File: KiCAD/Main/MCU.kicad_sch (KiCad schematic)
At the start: 26 parts, among them Q4 2N7002, SW1 RESET, SW2 USER, U4 STM32H750VBTx, Y2 SiT8008xx-2x-xxE (25MHz)

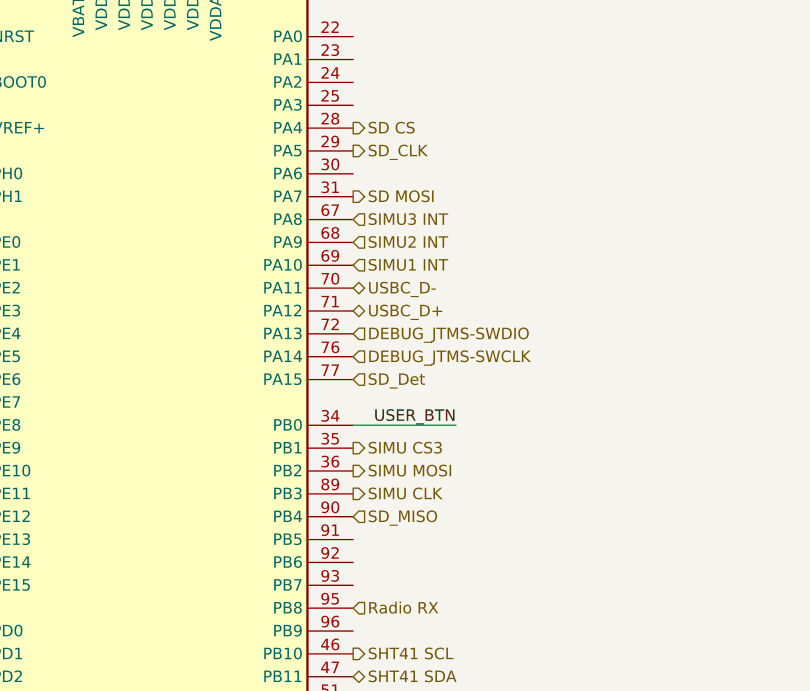
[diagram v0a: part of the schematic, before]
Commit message: Moved MISO1 to better position
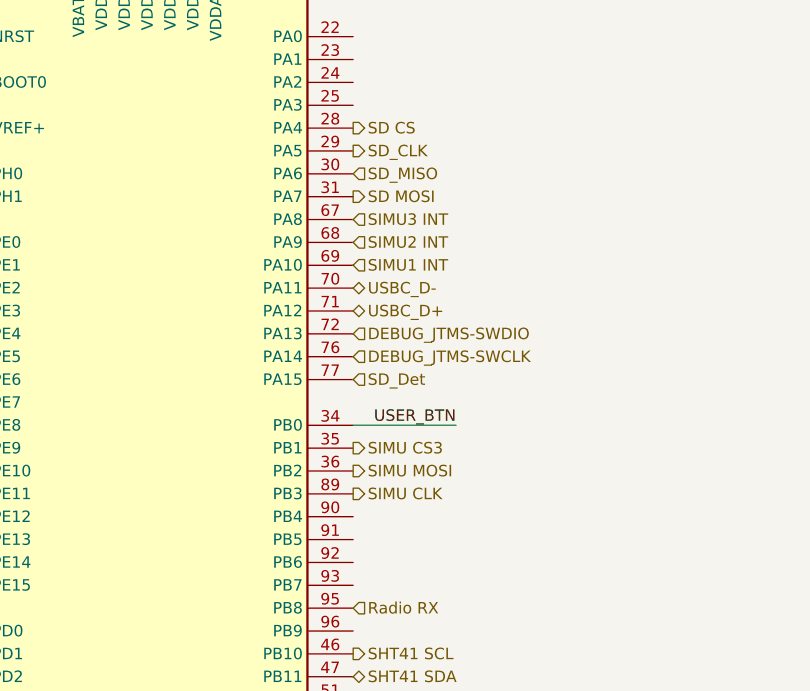
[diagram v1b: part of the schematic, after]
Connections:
- net SD_MISO: now also U4.30 (PA6); no longer U4.90 (PB4)
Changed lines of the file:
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@@
+		)
+	)
+	(hierarchical_label "SD_MISO"
+		(shape input)
+		(at 124.46 57.15 0)
+		(effects
+			(font
+				(size 1.27 1.27)
+			)
+			(justify left)
 		)
 	)
@@
 		(effects
 			(font
-				(size 1.27 1.27)
-			)
-			(justify left)
-		)
-	)
-	(hierarchical_label "SD_MISO"
-		(shape input)
-		(at 124.46 95.25 0)
-		(effects
-			(font

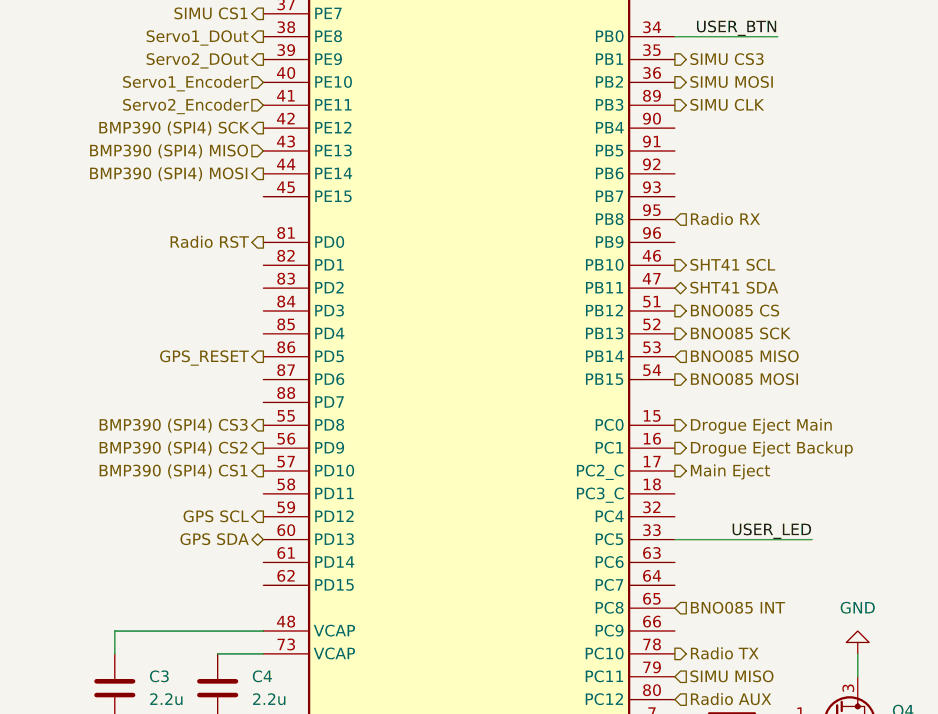
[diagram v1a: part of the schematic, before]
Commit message: Moved GPS I2C to more optimal location
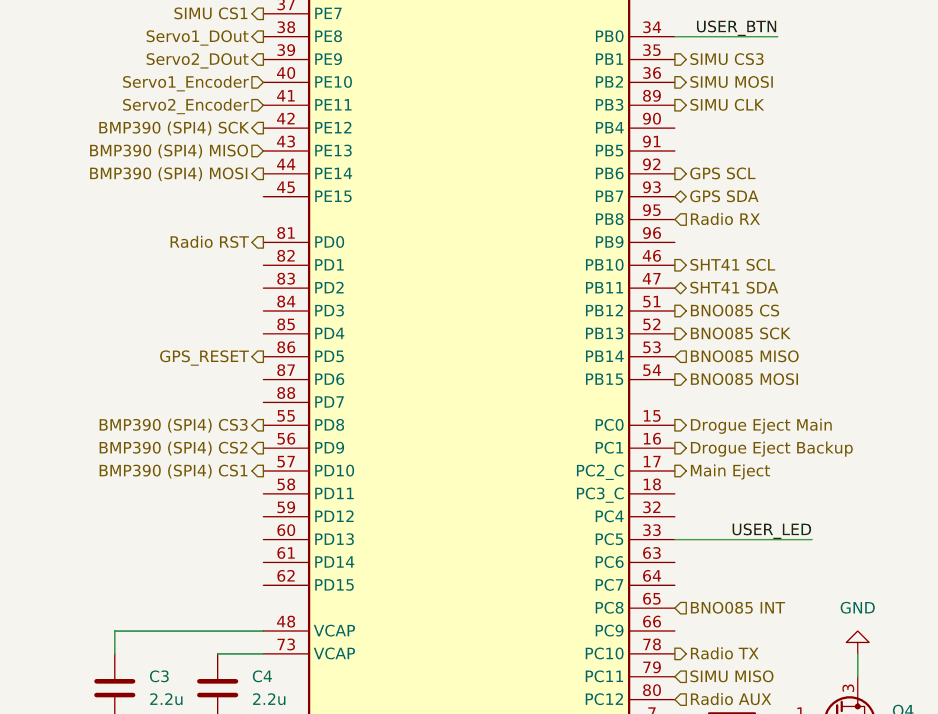
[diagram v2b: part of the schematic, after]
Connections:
- net GPS SCL: now also U4.92 (PB6); no longer U4.59 (PD12)
- net GPS SDA: now also U4.93 (PB7); no longer U4.60 (PD13)
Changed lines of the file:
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@@
-		)
-	)
-	(hierarchical_label "GPS SDA"
-		(shape bidirectional)
-		(at 78.74 140.97 180)
-		(effects
-			(font
-				(size 1.27 1.27)
-			)
-			(justify right)
 		)
 	)
@@
 		)
 	)
+	(hierarchical_label "GPS SCL"
+		(shape output)
+		(at 124.46 100.33 0)
+		(effects
+			(font
+				(size 1.27 1.27)
+			)
+			(justify left)
+		)
+	)
 	(hierarchical_label "BMP390 (SPI4) CS2"
 		(shape output)
@@
 		)
 	)
-	(hierarchical_label "GPS SCL"
-		(shape output)
-		(at 78.74 138.43 180)
-		(effects
-			(font
-				(size 1.27 1.27)
-			)
-			(justify right)
-		)
-	)
 	(hierarchical_label "SD_Det"
 		(shape input)
@@
 		)
 	)
+	(hierarchical_label "GPS SDA"
+		(shape bidirectional)
+		(at 124.46 102.87 0)
+		(effects
+			(font
+				(size 1.27 1.27)
+			)
+			(justify left)
+		)
+	)

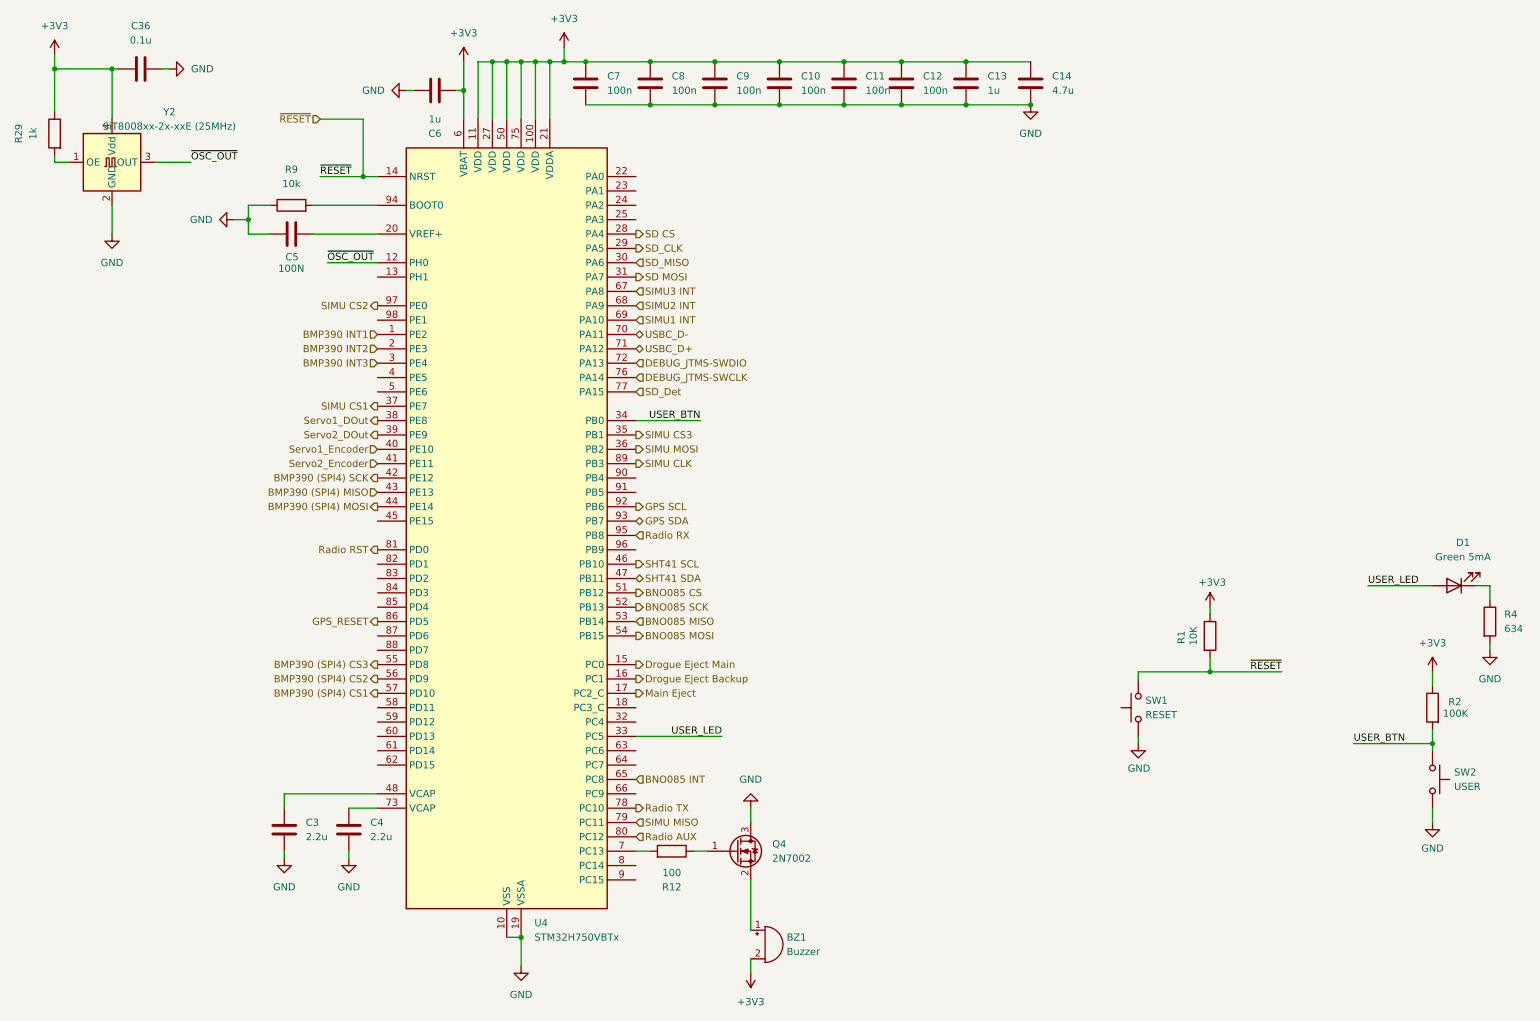
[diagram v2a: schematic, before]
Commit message: Moved around some more pins for easier routing
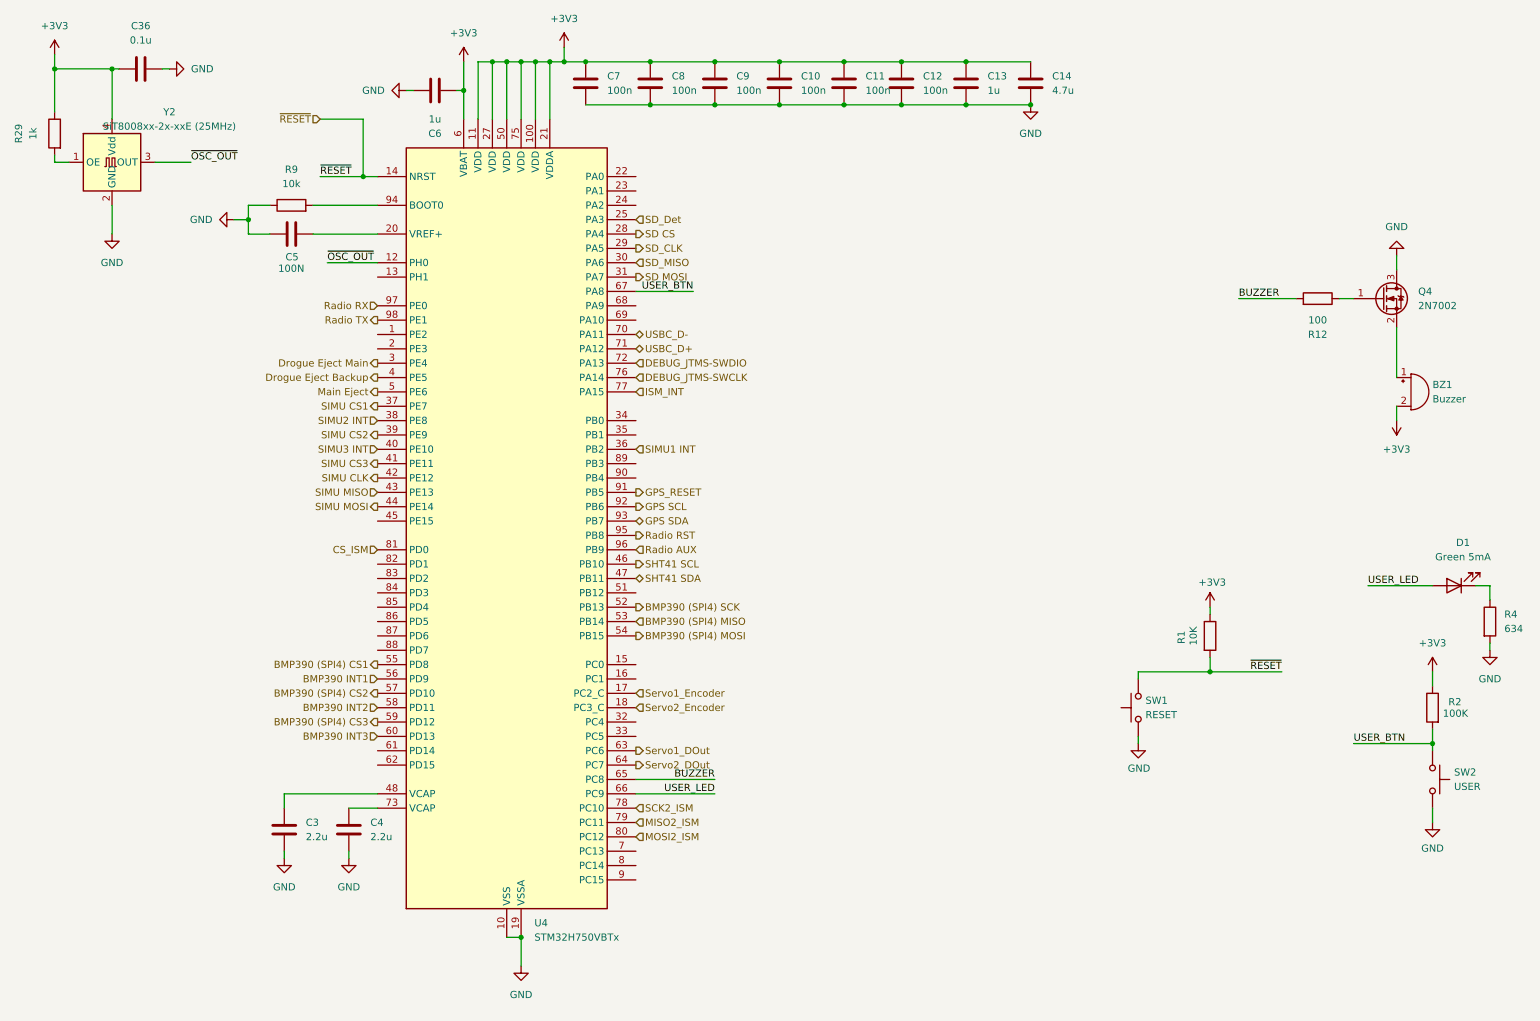
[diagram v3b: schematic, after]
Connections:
- net BNO085 MISO is gone; now on net BMP390 (SPI4) MISO: U4.53 (PB14)
- net BNO085 MOSI is gone; now on net BMP390 (SPI4) MOSI: U4.54 (PB15)
- net BNO085 SCK is gone; now on net BMP390 (SPI4) SCK: U4.52 (PB13)
- net BMP390 (SPI4) CS1: now also U4.55 (PD8); no longer U4.57 (PD10)
- net BMP390 (SPI4) CS2: now also U4.57 (PD10); no longer U4.56 (PD9)
- net BMP390 (SPI4) CS3: now also U4.59 (PD12); no longer U4.55 (PD8)
- net BMP390 (SPI4) MISO: no longer U4.43 (PE13)
- net BMP390 (SPI4) MOSI: no longer U4.44 (PE14)
- net BMP390 (SPI4) SCK: no longer U4.42 (PE12)
- net BMP390 INT1: now also U4.56 (PD9); no longer U4.1 (PE2)
- net BMP390 INT2: now also U4.58 (PD11); no longer U4.2 (PE3)
- net BMP390 INT3: now also U4.60 (PD13); no longer U4.3 (PE4)
- net Drogue Eject Backup: now also U4.4 (PE5); no longer U4.16 (PC1)
- net Drogue Eject Main: now also U4.3 (PE4); no longer U4.15 (PC0)
- net GPS_RESET: now also U4.91 (PB5); no longer U4.86 (PD5)
- net Main Eject: now also U4.5 (PE6); no longer U4.17 (PC2_C)
- net Radio AUX: now also U4.96 (PB9); no longer U4.80 (PC12)
- net Radio RST: now also U4.95 (PB8); no longer U4.81 (PD0)
- net Radio RX: now also U4.97 (PE0); no longer U4.95 (PB8)
- net Radio TX: now also U4.98 (PE1); no longer U4.78 (PC10)
- net SD_Det: now also U4.25 (PA3); no longer U4.77 (PA15)
- net SIMU CLK: now also U4.42 (PE12); no longer U4.89 (PB3)
- net SIMU CS2: now also U4.39 (PE9); no longer U4.97 (PE0)
- net SIMU CS3: now also U4.41 (PE11); no longer U4.35 (PB1)
- net SIMU MISO: now also U4.43 (PE13); no longer U4.79 (PC11)
- net SIMU MOSI: now also U4.44 (PE14); no longer U4.36 (PB2)
- net SIMU1 INT: now also U4.36 (PB2); no longer U4.69 (PA10)
- net SIMU2 INT: now also U4.38 (PE8); no longer U4.68 (PA9)
- net SIMU3 INT: now also U4.40 (PE10); no longer U4.67 (PA8)
- net Servo1_DOut: now also U4.63 (PC6); no longer U4.38 (PE8)
- net Servo1_Encoder: now also U4.17 (PC2_C); no longer U4.40 (PE10)
- net Servo2_DOut: now also U4.64 (PC7); no longer U4.39 (PE9)
- net Servo2_Encoder: now also U4.18 (PC3_C); no longer U4.41 (PE11)
- net USER_BTN: now also U4.67 (PA8); no longer U4.34 (PB0)
- net USER_LED: now also U4.66 (PC9); no longer U4.33 (PC5)
- net at U4.7 (PC13): no longer R12.2
- net BNO085 CS: no longer names the net of U4.51 (PB12)
- net BNO085 INT renamed BUZZER
- net BUZZER: now also R12.2
- new net CS_ISM: U4.81 (PD0)
- new net ISM_INT: U4.77 (PA15)
- new net MISO2_ISM: U4.79 (PC11)
- new net MOSI2_ISM: U4.80 (PC12)
- new net SCK2_ISM: U4.78 (PC10)
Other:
- moved on the sheet: BZ1, Q4, R12

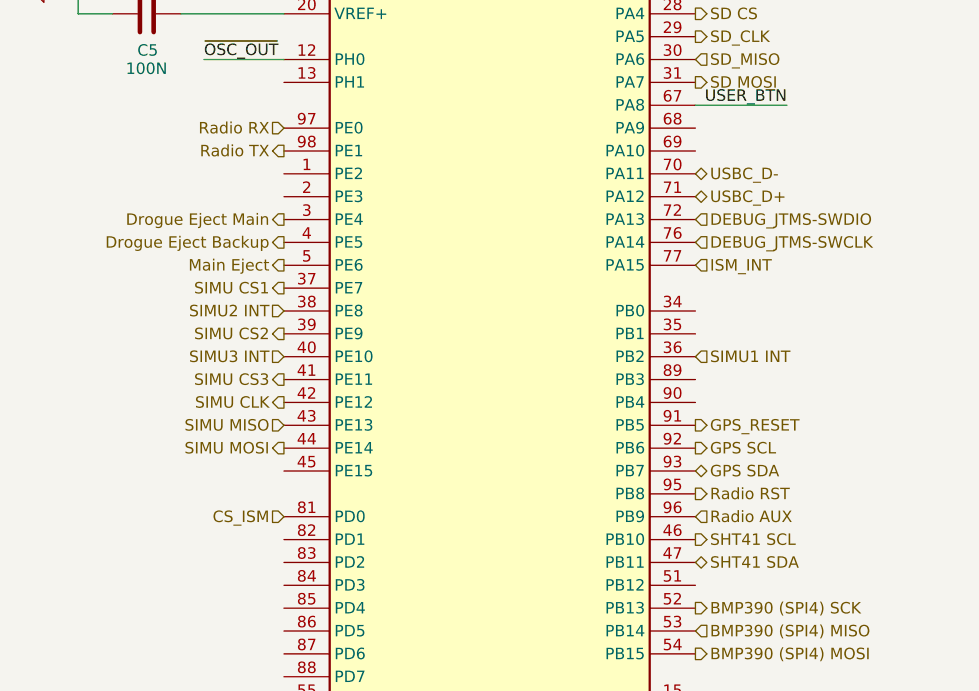
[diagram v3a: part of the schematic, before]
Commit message: Changed BMM350 for LIS2MDL
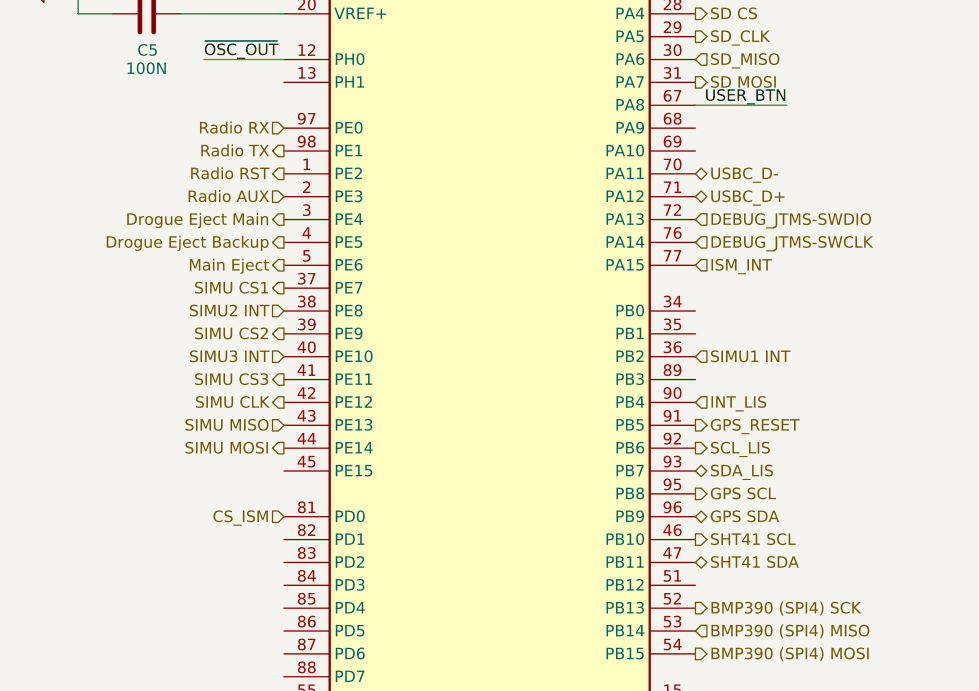
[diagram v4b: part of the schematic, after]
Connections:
- net GPS SCL: now also U4.95 (PB8); no longer U4.92 (PB6)
- net GPS SDA: now also U4.96 (PB9); no longer U4.93 (PB7)
- net Radio AUX: now also U4.2 (PE3); no longer U4.96 (PB9)
- net Radio RST: now also U4.1 (PE2); no longer U4.95 (PB8)
- net INT_LIS: now reaches U4.90 (PB4)
- new net SCL_LIS: U4.92 (PB6)
- new net SDA_LIS: U4.93 (PB7)
